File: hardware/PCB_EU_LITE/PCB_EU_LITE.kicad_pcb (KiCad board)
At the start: 4 copper layers, 100 x 100 mm, 165 parts, among them J101 24 V IN, J201 UART 3V3, J301 MEM2061 SPI, J401 SHT4x XH2.54-4P-90, J403 FLOAT / GND, J411 FAN1 2510-4P 90deg, J421 FAN2 2510-4P 90deg, J501 LED + / GND, J701 PTC + / RETURN, J702 PUMP + / RETURN, Q102 IRL2505, Q411 FAN1 AO3422, Q421 FAN2 AO3422, Q501 BSC146N10LS5, Q701 BC847B-DIO, Q702 BC857B, Q703 CSD19531KCS, Q704 AO3422, Q901 BC847B (R), Q902 BC847B (G), Q903 BC847B (B), SW201 RESET, SW202 BOOT, U101 ST1S14PHR, U102 INA238, U201 ST1S10PHR, U202 ESP32-WROOM-32E-N4, U301 MCP7940N, U401 USBLC6-2SC6, U501 LM3429MH/NOPB, Y301 32.768k CL7p

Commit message: Shorten LITE switch loop and connect ground islands
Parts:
- moved C204 18.8 mm to (33.8, 31.5), turned to 180 degrees
- moved L201 12.0 mm to (37.3, 32.0), turned to 90 degrees
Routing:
- net PUMP_GPIO: track 172.0 -> 123.7 mm, vias 6 -> 7
- net LOGIC_SW: track 20.2 -> 2.68 mm, vias 3 -> 0
- net SHT_SCL: track 152.5 -> 141.6 mm
- net +3V3: track 364.2 -> 354.0 mm, vias 21 -> 19
- net +12V: track 219.6 -> 212.7 mm, vias 6 -> 8
- net GND: track 767.4 -> 762.8 mm, vias 9 -> 12
- net PTC_PNP_B: track 27.9 -> 24.5 mm
- net LED_IS: track 60.4 -> 58.7 mm
- net PTC_NPN_C: track 16.1 -> 14.6 mm

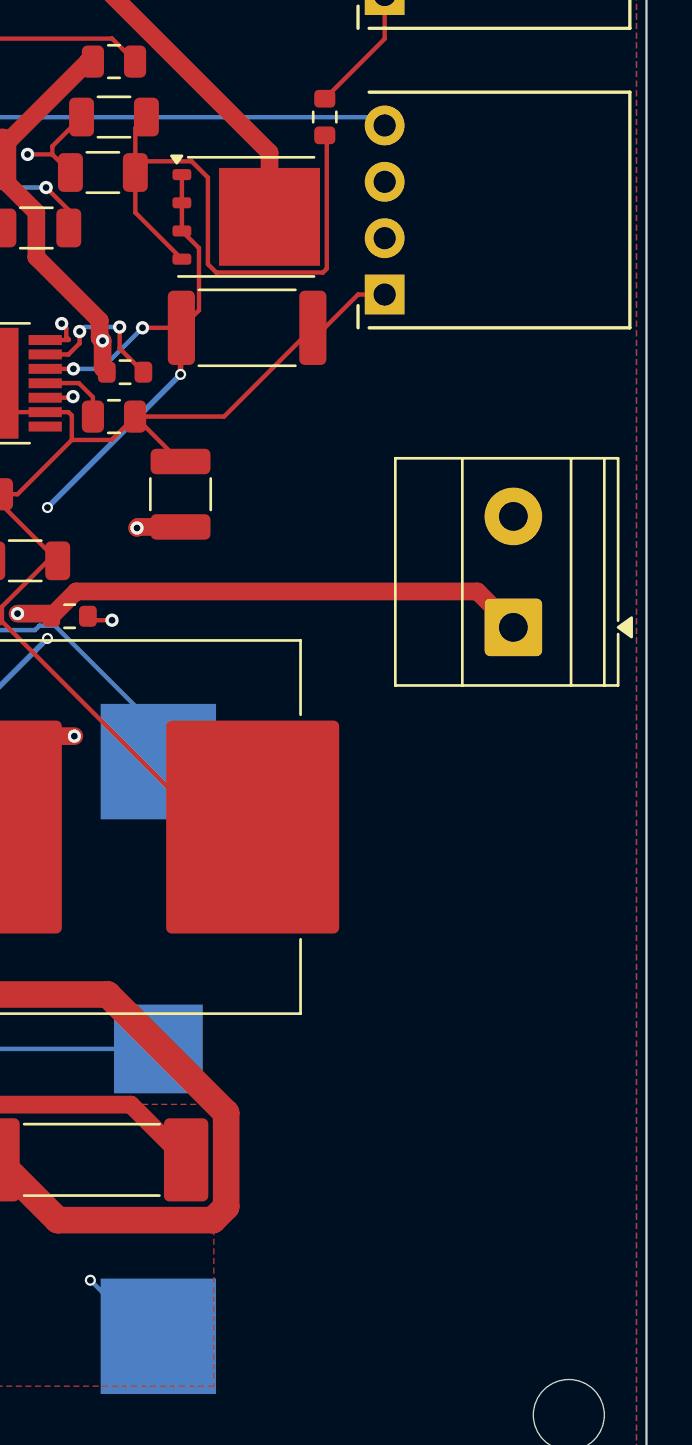
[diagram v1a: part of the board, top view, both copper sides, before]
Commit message: Finish EU-LITE LED routing and parallel outputs
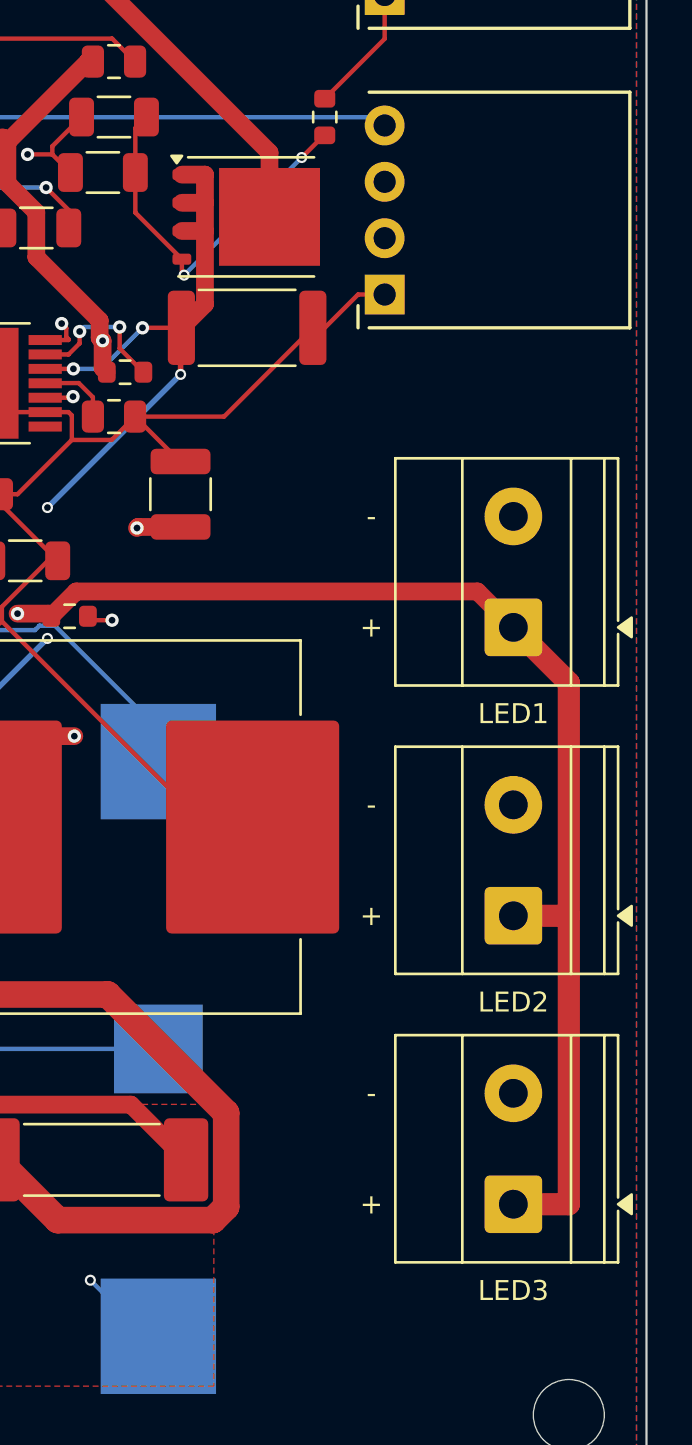
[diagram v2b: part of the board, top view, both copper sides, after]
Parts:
- added J502: LED 2 + / GND, TerminalBlock_Phoenix:TerminalBlock_Phoenix_MKDS-1,5-2_1x02_P5.00mm_Horizontal, F.Cu at (94.0, 74.0)
- added J503: LED 3 + / GND, TerminalBlock_Phoenix:TerminalBlock_Phoenix_MKDS-1,5-2_1x02_P5.00mm_Horizontal, F.Cu at (94.0, 87.0)
- R505: value 6k2 1% -> 4k7 1%
- R506: value 1k2 1% -> 620R 1%
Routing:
- net LED_POS: track 48.5 -> 80.5 mm
- net LED_GATE: track 26.8 -> 17.2 mm, vias 0 -> 2
- net LED_IS: track 58.7 -> 61.7 mm
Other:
- board text added: "+"
- board text added: "-"
- board text added: "LED1"
- board text added: "LED2"
- board text added: "LED3"
